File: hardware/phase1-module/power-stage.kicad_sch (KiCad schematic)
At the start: 42 parts, among them Q1 CSD18563Q5A, Q2 CSD18563Q5A, Q5 2N7002, Q6 2N7002, U3 LM5145RGYR

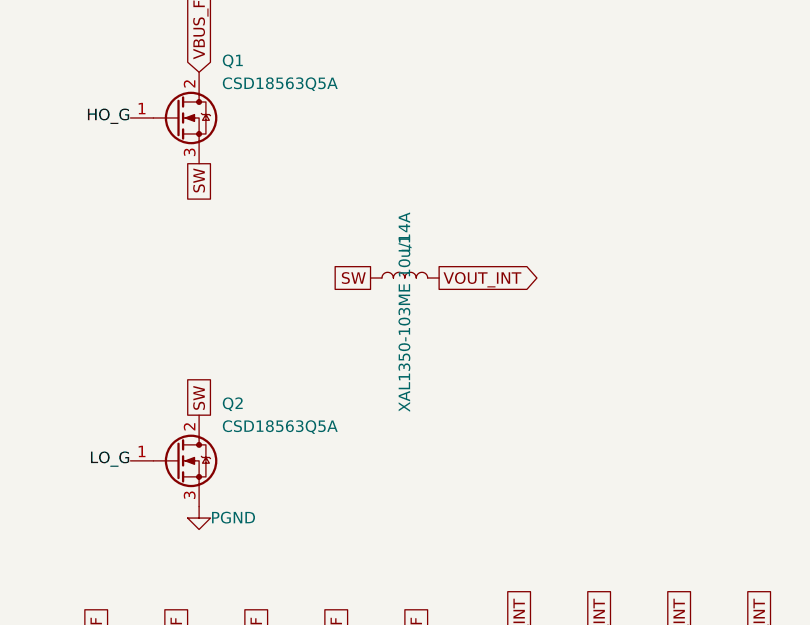
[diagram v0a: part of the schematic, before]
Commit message: Apply China-sourcing engineering changes across all boards + mechanical frame
All datasheet-verified before application (details hardware/SOURCING.md sF):
- TMUX1101 -> TS5A3166DBVR (LCSC availability; ts5a3166.pdf: pin POSITIONS
  identical - 1=NO 2=COM 3=GND 4=IN 5=V+; VIH 2.4V ok from 3.3V GPIO)
- TLV7011 DBVR -> DCKR: tlv7022.pdf shows DBV/DCK share one pinout, so
  footprint-only (SOT-353_SC-70-5); SOT-23-5 stock in China is nearly gone
- crystal load caps 10p -> 18p, both phases (CL=12pF China crystals; the
  HANDOVER-blessed alternative to hunting CL=8pF parts)
- Phase-1 inductor -> MWSA1707S-100MT (JLCPCB-verified 16.5A Isat/10.5A
  Irms vs 12A/8A required); value strings now dual-source Sunlord/Coilcraft
- module slot power + P2 output -> XT60PW-M (2-pin), backplane slots ->
  XT60PW-F; bus shunt -> 2x BVS-M-R0005 parallel (the exact-net checker
  caught RS1/RS2 placed one pin-span apart merging VBUS_IN into VBUS)
- 470u bulk -> THT radial D10; output MLCCs 22u -> 10u/50V X7S; buzzer ->
  MLT-8530 (fp placeholder)
All four checker chains green: 137/173/30/80 components.

hardware/MECHANICAL.md (frozen): 30mm slot pitch, P2 130x90 4-layer,
backplane ~330x100 2-layer 2oz, manager 100x80; cost-first stackup (1oz
outer + solder-reinforced bus, 2oz only if the thermal soak demands it);
inductor footprint = SUPERSET pattern accepting Sunlord 1707 AND Coilcraft
XAL1510 so the A/B pair is a pure part swap.

HANDOVER: sub-0.5V mV-accurate output DEFERRED to a future dedicated
linear post-regulator module (user decision 2026-07-18); buck floors
documented (P2 0.7V @30V bus, P1 0.5V).

Co-Authored-By: Claude Fable 5 <noreply@anthropic.com>
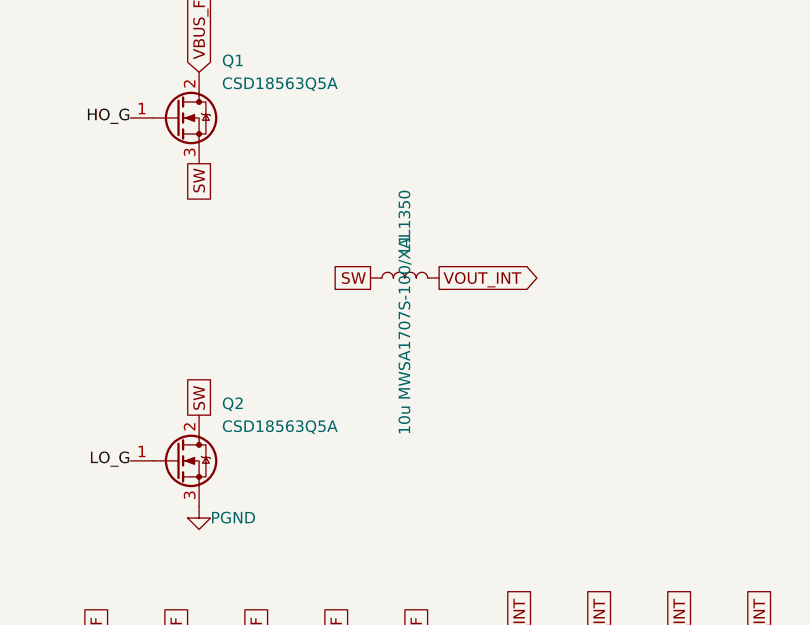
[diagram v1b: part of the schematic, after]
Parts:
- L1: value XAL1350-103ME 10u/14A -> 10u MWSA1707S-100/XAL1350
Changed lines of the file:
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@@
     (in_bom yes) (on_board yes) (dnp no)
     (property "Reference" "L1" (at 180.34 92.71 0) (effects (font (size 1.27 1.27))))
-    (property "Value" "XAL1350-103ME 10u/14A" (at 180.34 100.33 0) (effects (font (size 1.27 1.27))))
+    (property "Value" "10u MWSA1707S-100/XAL1350" (at 180.34 100.33 0) (effects (font (size 1.27 1.27))))
     (property "Footprint" "Inductor_SMD:L_Coilcraft_XAL1350-XXX" (at 180.34 96.52 0) (effects (font (size 1.27 1.27)) hide))
     (property "Datasheet" "~" (at 180.34 96.52 0) (effects (font (size 1.27 1.27)) hide))

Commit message: Footprint pass: China-part land patterns generated, placeholders retired
build_fplib.py sourcing_footprints() - geometry vetted from LCSC/EasyEDA
library pulls (easyeda2kicad), encoded in code like the PowerFET precedent
so regeneration needs no network:
- XT60PW-M / XT60PW-F: power pins 3.8mm pads / 2.9-2.8mm drills @ 7.2mm
  pitch + 0.6x1.6 retention slots. The -F library pull had the RETENTION
  LEGS numbered as pads 1,2 - power pads renumbered to 1,2 to match the -M
  and the Conn_01x02 symbol (a trap no netlist check would ever catch)
- L_1707_XAL1510: SUPERSET pad 5.39x13.2 @ +/-6.405 covering Sunlord
  MWSA1707S (3.5x12.8 @ 7.35) and Coilcraft XAL1510 (3.18x13.2 @ 5.3) -
  the A/B thermal pair and the P1 10uH are pure part swaps
- R3920_BVS bar shunt, MLT-8530 buzzer (edge pads paired 1,1/2,2)
Generators swapped off placeholders (P1 L1, P2 L1/L3/J1/J4, backplane
slots+RS pair, manager buzzer); all four chains green (137/173/30/80).

MECHANICAL.md: insertion geometry corrected to server-PSU style (vertical
rear backplane, modules slide horizontally; XT60 height stagger = power-
first mating). HARD GATE added: XT60 +/- pad mating is ASSUMED until a
mated pair is buzzed out on arrival - required before gerber submission.

Co-Authored-By: Claude Fable 5 <noreply@anthropic.com>
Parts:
- L1: footprint Inductor_SMD:L_Coilcraft_XAL1350-XXX -> labbench:L_1707_XAL1510
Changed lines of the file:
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@@
     (property "Reference" "L1" (at 180.34 92.71 0) (effects (font (size 1.27 1.27))))
     (property "Value" "10u MWSA1707S-100/XAL1350" (at 180.34 100.33 0) (effects (font (size 1.27 1.27))))
-    (property "Footprint" "Inductor_SMD:L_Coilcraft_XAL1350-XXX" (at 180.34 96.52 0) (effects (font (size 1.27 1.27)) hide))
+    (property "Footprint" "labbench:L_1707_XAL1510" (at 180.34 96.52 0) (effects (font (size 1.27 1.27)) hide))
     (property "Datasheet" "~" (at 180.34 96.52 0) (effects (font (size 1.27 1.27)) hide))
     (pin "1")

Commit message: Add LCSC part numbers to all four boards' schematics and generate BOMs
common/bom.py writes hidden LCSC/MPN/Manufacturer properties into the
placed symbols (additive only, both one-line and KiCad multi-line
property styles) and emits <board>/bom/<board>-bom.csv plus a
JLCPCB-format CSV. Part table in common/lcsc_parts.py, transcribed
from SOURCING.md with explicit references per board; CHECK notes flag
footprint/variant mismatches. --check fails on stale output.

Co-Authored-By: Claude Opus 5.5 (1M context) <noreply@anthropic.com>
Claude-Session: https://claude.ai/code/session_01MKtKgebN9BpUrgqHq9t7pT
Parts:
- L1: LCSC (none) -> C5240401; MPN (none) -> MWSA1707S-100MT; Manufacturer (none) -> Sunlord
- Q1, Q2: LCSC (none) -> C77239; MPN (none) -> CSD18563Q5A; Manufacturer (none) -> TI
- U3: LCSC (none) -> C485912; MPN (none) -> LM5145RGYR; Manufacturer (none) -> TI
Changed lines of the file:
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@@
     (property "Footprint" "labbench:LM5145_RGY0020B" (at 76.2 106.68 0) (effects (font (size 1.27 1.27)) hide))
     (property "Datasheet" "~" (at 76.2 106.68 0) (effects (font (size 1.27 1.27)) hide))
+    (property "LCSC" "C485912" (at 76.2 106.68 0) (effects (font (size 1.27 1.27)) hide))
+    (property "MPN" "LM5145RGYR" (at 76.2 106.68 0) (effects (font (size 1.27 1.27)) hide))
+    (property "Manufacturer" "TI" (at 76.2 106.68 0) (effects (font (size 1.27 1.27)) hide))
     (pin "1")
     (pin "10")
@@
     (property "Footprint" "labbench:PowerFET_SON5x6_GDS" (at 154.94 78.74 0) (effects (font (size 1.27 1.27)) hide))
     (property "Datasheet" "~" (at 154.94 78.74 0) (effects (font (size 1.27 1.27)) hide))
+    (property "LCSC" "C77239" (at 154.94 78.74 0) (effects (font (size 1.27 1.27)) hide))
+    (property "MPN" "CSD18563Q5A" (at 154.94 78.74 0) (effects (font (size 1.27 1.27)) hide))
+    (property "Manufacturer" "TI" (at 154.94 78.74 0) (effects (font (size 1.27 1.27)) hide))
     (pin "1")
     (pin "2")
@@
     (property "Footprint" "labbench:PowerFET_SON5x6_GDS" (at 154.94 116.84 0) (effects (font (size 1.27 1.27)) hide))
     (property "Datasheet" "~" (at 154.94 116.84 0) (effects (font (size 1.27 1.27)) hide))
+    (property "LCSC" "C77239" (at 154.94 116.84 0) (effects (font (size 1.27 1.27)) hide))
+    (property "MPN" "CSD18563Q5A" (at 154.94 116.84 0) (effects (font (size 1.27 1.27)) hide))
+    (property "Manufacturer" "TI" (at 154.94 116.84 0) (effects (font (size 1.27 1.27)) hide))
     (pin "1")
     (pin "2")
@@
     (property "Footprint" "labbench:L_1707_XAL1510" (at 180.34 96.52 0) (effects (font (size 1.27 1.27)) hide))
     (property "Datasheet" "~" (at 180.34 96.52 0) (effects (font (size 1.27 1.27)) hide))
-    (pin "1")
-    (pin "2")
+    (property "LCSC" "C5240401" (at 180.34 96.52 0) (effects (font (size 1.27 1.27)) hide))
+    (property "MPN" "MWSA1707S-100MT" (at 180.34 96.52 0) (effects (font (size 1.27 1.27)) hide))
+    (property "Manufacturer" "Sunlord" (at 180.34 96.52 0) (effects (font (size 1.27 1.27)) hide))
+    (pin "1")
+    (pin "2")

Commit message: Phase-1 BOM: LCSC numbers for every assembled part
Fill the 109 missing Phase-1 placements from the JLCPCB catalogue
(checked 2026-09-27, Basic parts where one fits), so 127 of 136
placements carry an LCSC number. J1-J6 and F1 stay hand-solder;
C17 and R17 are DNP.

Out-of-stock swaps: Q1-Q4 CSD18563Q5A -> NTMFS5C670NLT1G (SO-8FL,
same pinout), P1 U5 INA228AIDGSR -> INA228AQDGSRQ1. Y1 moves to the
CL = 12 pF version of the same crystal (C400090 was the 10 pF one).

Co-Authored-By: Claude Opus 5.5 (1M context) <noreply@anthropic.com>
Claude-Session: https://claude.ai/code/session_013uVohQZFdivAh43gw4mZtf
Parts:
- C18: LCSC (none) -> C1622; MPN (none) -> CL10B473KB8NNNC; Manufacturer (none) -> Samsung Electro-Mechanics
- C19: LCSC (none) -> C1644; MPN (none) -> CL10C150JB8NNNC; Manufacturer (none) -> Samsung Electro-Mechanics
- C20, C75, C76, C77: LCSC (none) -> C77102; MPN (none) -> GRM32ER71H106KA12L; Manufacturer (none) -> Murata Electronics
- C21: LCSC (none) -> C2887271; MPN (none) -> RVT220UF50V67RV0021; Manufacturer (none) -> KNSCHA
- C22, C78: LCSC (none) -> C46550471; MPN (none) -> MA35V220M8X12; Manufacturer (none) -> jieerrui
- C23, C79, C80, C81: LCSC (none) -> C5341638; MPN (none) -> CC1210KKX7R8BB226; Manufacturer (none) -> YAGEO
- C24: LCSC (none) -> C1322360; MPN (none) -> 0603B822K500NT; Manufacturer (none) -> FH
- C25: LCSC (none) -> C1643; MPN (none) -> 0603CG121J500NT; Manufacturer (none) -> FH
- C26: LCSC (none) -> C1613; MPN (none) -> CL10B332KB8NNNC; Manufacturer (none) -> Samsung Electro-Mechanics
- C27, C28: LCSC (none) -> C14663; MPN (none) -> CC0603KRX7R9BB104; Manufacturer (none) -> YAGEO
- C29: LCSC (none) -> C23630; MPN (none) -> CL10A225KO8NNNC; Manufacturer (none) -> Samsung Electro-Mechanics
- D3, D4: LCSC (none) -> C77328; MPN (none) -> BAT54W; Manufacturer (none) -> Jiangsu Changjing Electronics Technology Co., Ltd.
- Q1, Q2: LCSC C77239 -> C179626; MPN CSD18563Q5A -> NTMFS5C670NLT1G; Manufacturer TI -> onsemi
- Q5, Q6: LCSC (none) -> C8545; MPN (none) -> 2N7002; Manufacturer (none) -> Jiangsu Changjing Electronics Technology Co., Ltd.
- R16, R18, R19, R20, R22, R23: LCSC (none) -> C25803; MPN (none) -> 0603WAF1003T5E; Manufacturer (none) -> UNI-ROYAL
- R21: LCSC (none) -> C22797; MPN (none) -> 0603WAF1302T5E; Manufacturer (none) -> UNI-ROYAL
- R24: LCSC (none) -> C25981; MPN (none) -> 0603WAF8201T5E; Manufacturer (none) -> UNI-ROYAL
- R25: LCSC (none) -> C21190; MPN (none) -> 0603WAF1001T5E; Manufacturer (none) -> UNI-ROYAL
- R26: LCSC (none) -> C22928; MPN (none) -> 0603WAF2872T5E; Manufacturer (none) -> UNI-ROYAL
- R27: LCSC (none) -> C421608; MPN (none) -> 25121WF2201T4E; Manufacturer (none) -> UNI-ROYAL
- R28: LCSC (none) -> C227839; MPN (none) -> AC0603FR-07365RL; Manufacturer (none) -> YAGEO
- R29: LCSC (none) -> C23164; MPN (none) -> 0603WAF470KT5E; Manufacturer (none) -> UNI-ROYAL

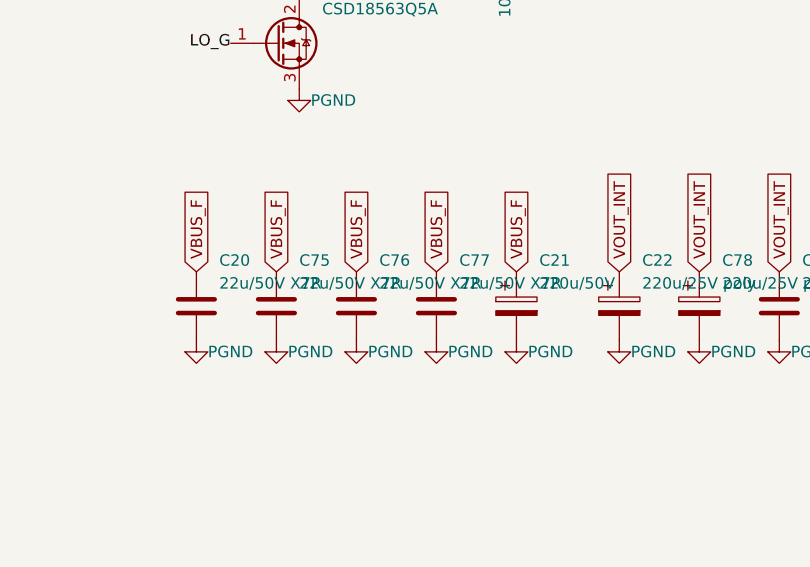
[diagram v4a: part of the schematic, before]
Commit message: Phase-1/2 L2 to the 5x5 mm land; close the last BOM CHECK rows
Phase-1 and phase-2 L2 (33u/1.2A aux-buck inductor) sat on 1210 lands,
and no stocked 1210 33 uH is rated above 0.5 A. Both now use the
manager's part, cjiang FNR5040S330MT (C167973, Isat 1.30 A min), on
L_Changjiang_FNR5040S, as an ECO on each routed board:
- phase-1: L2 at (32.6, 61.25); the SW_AUX diagonal is re-ended on the
  new pad and a 0.4 mm F.Cu 5V0 link joins L2's via to C54's.
- phase-2: L2 at (68.4, 57.45) r270; its SW_AUX and 5V0 vias now sit in
  the pads, the two stubs that reached them are gone, and a 0.3 mm stub
  ties C55's 5V0 via to pad 2.
- common/eco_swap_fp.py does the in-place footprint swap (nets, fields
  and path carried over). sheets_common.py, both gen_board.py PLACEMENT
  tables and the aux-rails sheets carry the change, so a rebuild matches.
- DRC unchanged: phase-1 10 silk warnings, phase-2 19 warnings, 0 errors
  and 0 unconnected on both. Fab zips, BOMs and CPLs regenerated.

The other CHECK rows (stock checked 2026-10-06):
- Phase-1 C20/C75-C77: no 22 uF 50 V 1210 is stocked, so the design
  value is now 10u/50V X7R (~0.3 Vpp input ripple at 8 A, 350 kHz).
- Phase-1 Q1-Q4: CSD18563Q5A still out of stock; NTMFS5C670NLT1G stays.
  Its case 488AA terminals land within 0.14 mm of the TI part's on the
  Q5A land.
- Phase-2 U3: LM5143QRHARQ1 is the LM5143A-Q1, same pin map; RHA0040N
  matches the RHA0040P land (EP 3.3, 0.5 pitch, 5.8 span).

No CHECK row is left in any BOM. INA228AQDGSRQ1 stock is down to 5, now
on the order-early list. README, HANDOVER, SOURCING, the build guide and
the tools READMEs are updated.

Co-Authored-By: Claude Opus 5.5 (1M context) <noreply@anthropic.com>
Claude-Session: https://claude.ai/code/session_01Kap1Vqs6wqd3fshJdnERW7
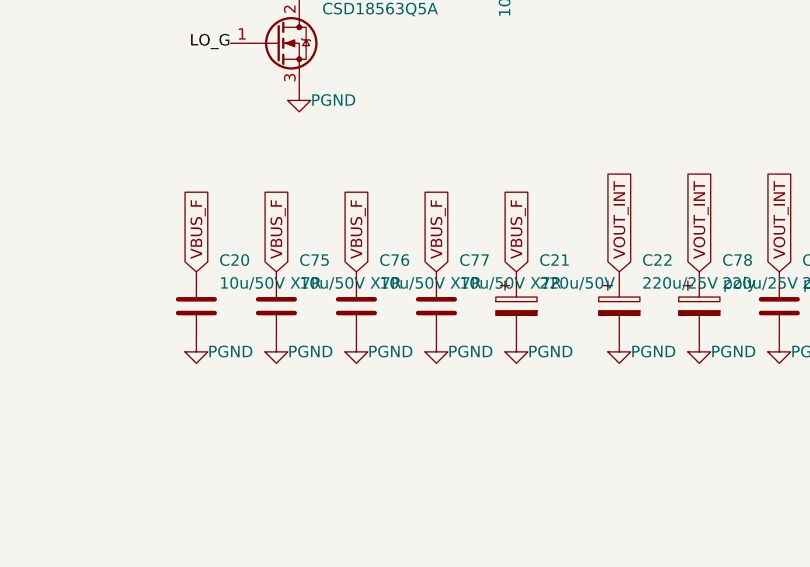
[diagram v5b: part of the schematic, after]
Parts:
- C20, C75, C76, C77: value 22u/50V X7R -> 10u/50V X7R
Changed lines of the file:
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@@
     (in_bom yes) (on_board yes) (dnp no)
     (property "Reference" "C20" (at 148.59 140.97 0) (effects (font (size 1.27 1.27)) (justify left)))
-    (property "Value" "22u/50V X7R" (at 148.59 143.51000000000002 0) (effects (font (size 1.27 1.27)) (justify left)))
+    (property "Value" "10u/50V X7R" (at 148.59 143.51000000000002 0) (effects (font (size 1.27 1.27)) (justify left)))
     (property "Footprint" "Capacitor_SMD:C_1210_3225Metric" (at 146.05 146.05 0) (effects (font (size 1.27 1.27)) hide))
     (property "Datasheet" "~" (at 146.05 146.05 0) (effects (font (size 1.27 1.27)) hide))
@@
     (in_bom yes) (on_board yes) (dnp no)
     (property "Reference" "C75" (at 157.48 140.97 0) (effects (font (size 1.27 1.27)) (justify left)))
-    (property "Value" "22u/50V X7R" (at 157.48 143.51000000000002 0) (effects (font (size 1.27 1.27)) (justify left)))
+    (property "Value" "10u/50V X7R" (at 157.48 143.51000000000002 0) (effects (font (size 1.27 1.27)) (justify left)))
     (property "Footprint" "Capacitor_SMD:C_1210_3225Metric" (at 154.94 146.05 0) (effects (font (size 1.27 1.27)) hide))
     (property "Datasheet" "~" (at 154.94 146.05 0) (effects (font (size 1.27 1.27)) hide))
@@
     (in_bom yes) (on_board yes) (dnp no)
     (property "Reference" "C76" (at 166.37 140.97 0) (effects (font (size 1.27 1.27)) (justify left)))
-    (property "Value" "22u/50V X7R" (at 166.37 143.51000000000002 0) (effects (font (size 1.27 1.27)) (justify left)))
+    (property "Value" "10u/50V X7R" (at 166.37 143.51000000000002 0) (effects (font (size 1.27 1.27)) (justify left)))
     (property "Footprint" "Capacitor_SMD:C_1210_3225Metric" (at 163.83 146.05 0) (effects (font (size 1.27 1.27)) hide))
     (property "Datasheet" "~" (at 163.83 146.05 0) (effects (font (size 1.27 1.27)) hide))
@@
     (in_bom yes) (on_board yes) (dnp no)
     (property "Reference" "C77" (at 175.26 140.97 0) (effects (font (size 1.27 1.27)) (justify left)))
-    (property "Value" "22u/50V X7R" (at 175.26 143.51000000000002 0) (effects (font (size 1.27 1.27)) (justify left)))
+    (property "Value" "10u/50V X7R" (at 175.26 143.51000000000002 0) (effects (font (size 1.27 1.27)) (justify left)))
     (property "Footprint" "Capacitor_SMD:C_1210_3225Metric" (at 172.72 146.05 0) (effects (font (size 1.27 1.27)) hide))
     (property "Datasheet" "~" (at 172.72 146.05 0) (effects (font (size 1.27 1.27)) hide))
